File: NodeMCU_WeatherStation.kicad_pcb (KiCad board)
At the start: 2 copper layers, 75 x 93.5 mm, 24 parts, among them J1 AVR-ISP-6, J2 Conn_01x15, J3 Conn_01x15, J4 Conn_01x04, J5 Conn_01x04, U1 BME280, U2 ATmega328P-AU, U3 TLC555CD, Y1 16MHz

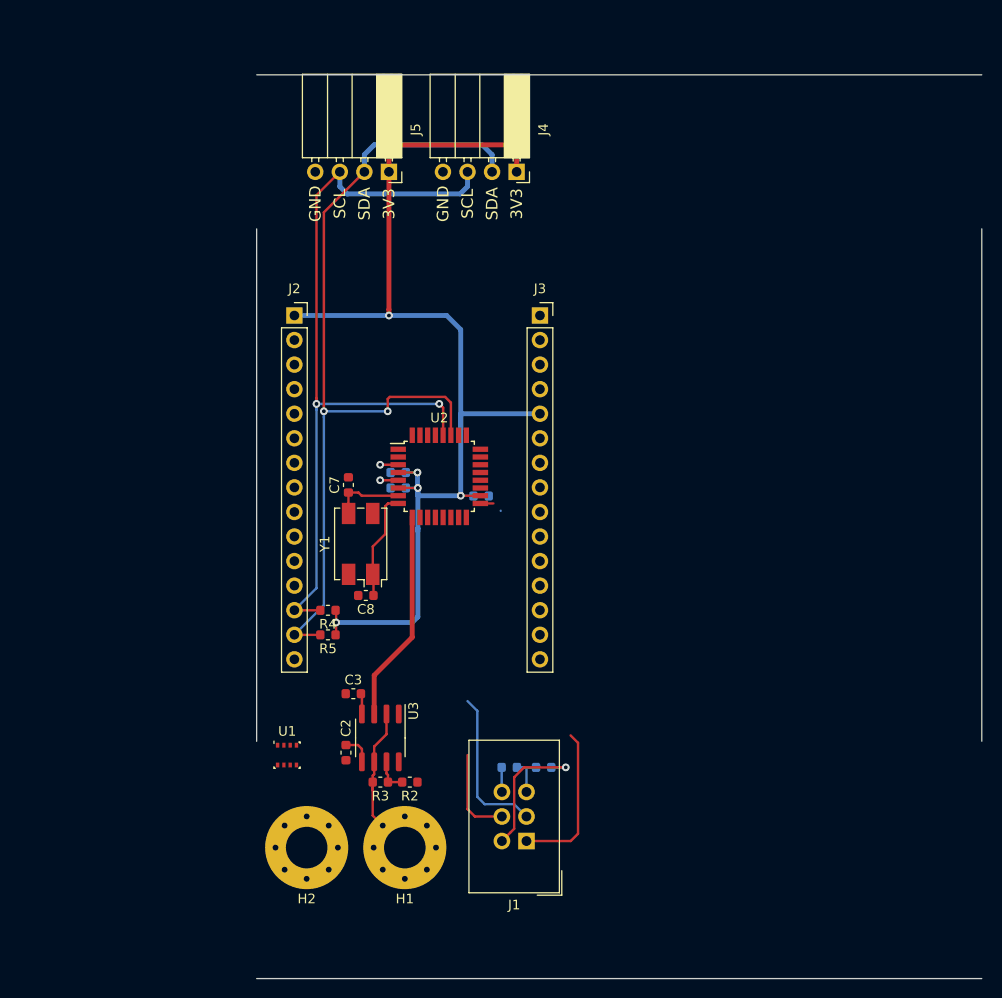
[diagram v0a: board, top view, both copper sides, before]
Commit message: added 4-20mA input and PT100 readout
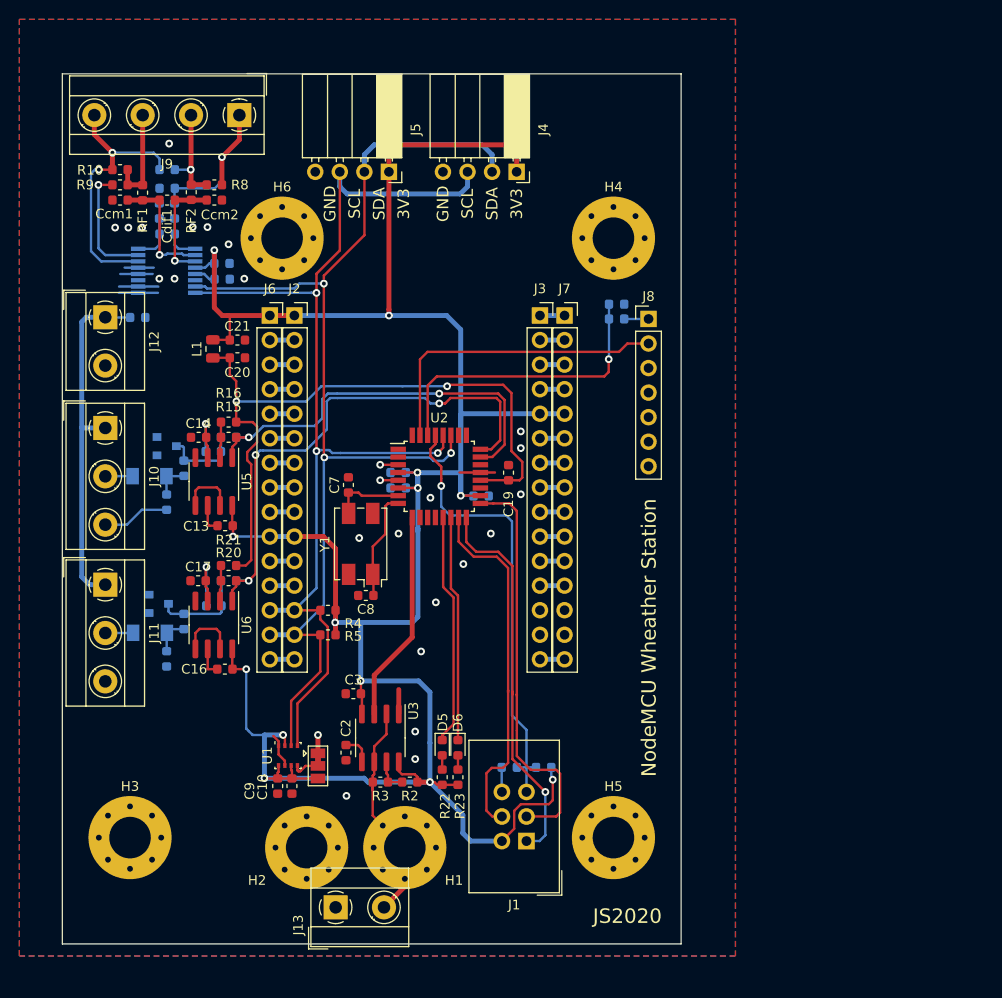
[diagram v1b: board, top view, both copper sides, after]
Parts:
- added C10: 100n, Capacitor_SMD:C_0603_1608Metric, F.Cu at (89.7, 128.7)
- added C11: 100n, Capacitor_SMD:C_0603_1608Metric, B.Cu at (82.5, 74.6)
- added C12: 100n, Capacitor_SMD:C_0603_1608Metric, B.Cu at (82.5, 76.2)
- added C13: 100n, Capacitor_SMD:C_0603_1608Metric, F.Cu at (82.8, 101.7)
- added C14: 100n, Capacitor_SMD:C_0603_1608Metric, F.Cu at (80.1, 92.6)
- added C15: 100n, Capacitor_SMD:C_0603_1608Metric, B.Cu at (83.2, 92.6)
- added C16: 100n, Capacitor_SMD:C_0603_1608Metric, F.Cu at (82.8, 116.6)
- added C17: 100n, Capacitor_SMD:C_0603_1608Metric, F.Cu at (80.0, 107.4)
- added C18: 100n, Capacitor_SMD:C_0603_1608Metric, B.Cu at (83.2, 107.4)
- added C19: 100n, Capacitor_SMD:C_0603_1608Metric, F.Cu at (112.1, 96.3)
- added C20: 100n, Capacitor_SMD:C_0603_1608Metric, F.Cu at (84.1, 84.4)
- added C21: 100n, Capacitor_SMD:C_0603_1608Metric, F.Cu at (84.1, 82.5)
- added C22: 100n, Capacitor_SMD:C_0603_1608Metric, B.Cu at (73.8, 80.2)
- added C9: 100n, Capacitor_SMD:C_0603_1608Metric, F.Cu at (88.3, 128.7)
- added Ccm1: 10n, Capacitor_SMD:C_0603_1608Metric, F.Cu at (72.0, 68.1)
- added Ccm2: 10n, Capacitor_SMD:C_0603_1608Metric, F.Cu at (81.7, 68.1)
- added Cdif1: 100n, Capacitor_SMD:C_0603_1608Metric, F.Cu at (76.8, 68.1)
- added Cdif2: 100n, Capacitor_SMD:C_0603_1608Metric, B.Cu at (76.8, 71.6)
- added D1: LL4148, Diode_SMD:D_MiniMELF, B.Cu at (75.0, 96.6)
- added D2: BZX84Cxx, Diode_SMD:D_SOT-23_ANK, B.Cu at (76.8, 93.5)
- added D3: LL4148, Diode_SMD:D_MiniMELF, B.Cu at (75.1, 112.8)
- added D4: BZX84Cxx, Diode_SMD:D_SOT-23_ANK, B.Cu at (76.0, 109.8)
- added D5: LED, LED_SMD:LED_0603_1608Metric, F.Cu at (105.3, 124.7)
- added D6: LED, LED_SMD:LED_0603_1608Metric, F.Cu at (106.9, 124.7)
- added H3: MountingHole_Pad, MountingHole:MountingHole_4.3mm_M4_Pad_Via, F.Cu at (73.0, 134.0)
- added H4: MountingHole_Pad, MountingHole:MountingHole_4.3mm_M4_Pad_Via, F.Cu at (123.0, 72.0)
- added H5: MountingHole_Pad, MountingHole:MountingHole_4.3mm_M4_Pad_Via, F.Cu at (123.0, 134.0)
- added H6: MountingHole_Pad, MountingHole:MountingHole_4.3mm_M4_Pad_Via, F.Cu at (88.7, 72.0)
- added J10: Screw_Terminal_01x03, TerminalBlock_MetzConnect:TerminalBlock_MetzConnect_Type055_RT01503HDWU_1x03_P5.00mm_Horizontal, F.Cu at (70.4, 91.6)
- added J11: Screw_Terminal_01x03, TerminalBlock_MetzConnect:TerminalBlock_MetzConnect_Type055_RT01503HDWU_1x03_P5.00mm_Horizontal, F.Cu at (70.4, 107.8)
- added J12: Screw_Terminal_01x02, TerminalBlock_MetzConnect:TerminalBlock_MetzConnect_Type055_RT01502HDWU_1x02_P5.00mm_Horizontal, F.Cu at (70.4, 80.2)
- added J13: Screw_Terminal_01x02, TerminalBlock_MetzConnect:TerminalBlock_MetzConnect_Type055_RT01502HDWU_1x02_P5.00mm_Horizontal, F.Cu at (94.3, 141.2)
- added J6: Conn_01x15, Connector_PinSocket_2.54mm:PinSocket_1x15_P2.54mm_Vertical, F.Cu at (87.5, 80.0)
- added J7: Conn_01x15, Connector_PinSocket_2.54mm:PinSocket_1x15_P2.54mm_Vertical, F.Cu at (117.9, 80.0)
- added J8: Conn_01x07, Connector_PinHeader_2.54mm:PinHeader_1x07_P2.54mm_Vertical, F.Cu at (126.6, 80.4)
- added J9: Screw_Terminal_01x04, TerminalBlock_MetzConnect:TerminalBlock_MetzConnect_Type055_RT01504HDWU_1x04_P5.00mm_Horizontal, F.Cu at (84.3, 59.3)
- added JP1: SolderJumper_3_Bridged12, Jumper:SolderJumper-3_P1.3mm_Bridged12_Pad1.0x1.5mm, F.Cu at (92.4, 126.6)
- added L1: L, Inductor_SMD:L_0805_2012Metric, F.Cu at (81.6, 83.5)
- added R10: n.b. (0R), Resistor_SMD:R_0603_1608Metric, F.Cu at (72.0, 64.9)
- added R11: n.b. (0R), Resistor_SMD:R_0603_1608Metric, B.Cu at (76.8, 64.9)
- added R12: 160, Resistor_SMD:R_0603_1608Metric, B.Cu at (76.8, 99.3)
- added R13: 100k, Resistor_SMD:R_0603_1608Metric, B.Cu at (78.6, 95.8)
- added R14: 100k, Resistor_SMD:R_0603_1608Metric, B.Cu at (81.6, 94.1)
- added R15: 15k, Resistor_SMD:R_0603_1608Metric, F.Cu at (83.2, 92.6)
- added R16: 75k, Resistor_SMD:R_0603_1608Metric, F.Cu at (83.2, 91.0)
- added R17: 160, Resistor_SMD:R_0603_1608Metric, B.Cu at (76.8, 115.5)
- added R18: 100k, Resistor_SMD:R_0603_1608Metric, B.Cu at (78.6, 111.6)
- added R19: 100k, Resistor_SMD:R_0603_1608Metric, B.Cu at (81.7, 110.0)
- added R20: 15k, Resistor_SMD:R_0603_1608Metric, F.Cu at (83.2, 107.4)
- added R21: 75k, Resistor_SMD:R_0603_1608Metric, F.Cu at (83.2, 105.9)
- added R22: R, Resistor_SMD:R_0603_1608Metric, F.Cu at (105.3, 127.8)
- added R23: R, Resistor_SMD:R_0603_1608Metric, F.Cu at (106.9, 127.8)
- added R6: 1k, Resistor_SMD:R_0603_1608Metric, B.Cu at (123.3, 80.4)
- added R7: 2k2, Resistor_SMD:R_0603_1608Metric, B.Cu at (123.3, 78.8)
- added R8: n.b. (0R), Resistor_SMD:R_0603_1608Metric, F.Cu at (81.7, 66.5)
- added R9: n.b. (0R), Resistor_SMD:R_0603_1608Metric, F.Cu at (72.0, 66.5)
- added RF1: 470, Resistor_SMD:R_0603_1608Metric, F.Cu at (74.3, 67.3)
- added RF2: 470, Resistor_SMD:R_0603_1608Metric, F.Cu at (79.3, 67.2)
- added RF3: 470, Resistor_SMD:R_0603_1608Metric, B.Cu at (77.6, 69.2)
- added RF4: 470, Resistor_SMD:R_0603_1608Metric, B.Cu at (76.0, 69.2)
- added Rref1: R, Resistor_SMD:R_0603_1608Metric, B.Cu at (76.8, 66.8)
- added U4: ADS122C04IPW, Package_SO:TSSOP-16_4.4x5mm_P0.65mm, B.Cu at (76.8, 75.4)
- added U5: LT1492, Package_SO:SOIC-8_3.9x4.9mm_P1.27mm, F.Cu at (81.7, 97.2)
- added U6: LT1492, Package_SO:SOIC-8_3.9x4.9mm_P1.27mm, F.Cu at (81.7, 112.0)
- moved U1 0.11 mm to (89.3, 125.5)
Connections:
- net Net-(U2-Pad25) renamed /I2C Water Sensor/ADC2
- net Net-(U2-Pad26) renamed /I2C Water Sensor/ADC3
- U1 pad 1: Net-(U1-Pad1) -> GND
- U1 pad 2: Net-(U1-Pad2) -> +3V3
- U1 pad 3: Net-(U1-Pad3) -> /SDA
- U1 pad 4: Net-(U1-Pad4) -> /SCL
- U1 pad 6: Net-(U1-Pad6) -> +3V3
- U1 pad 7: Net-(U1-Pad7) -> GND
- U1 pad 8: Net-(U1-Pad8) -> +3V3
- U2 pad 20: Net-(U2-Pad20) -> /4to20in 1/Vref
- U2 pad 23: Net-(U2-Pad23) -> /I2C Water Sensor/ADC0
- U2 pad 24: Net-(U2-Pad24) -> /I2C Water Sensor/ADC1
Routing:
- net +3V3: track 135.3 -> 276.3 mm, vias 6 -> 13
- net /4to20in 1/Vref: track 0.00 -> 70.4 mm, vias 0 -> 2
- net /I2C Water Sensor/ADC1: track 0.00 -> 54.6 mm, vias 0 -> 3
- net GND: track 6.50 -> 55.8 mm, vias 2 -> 26
- net /I2C Water Sensor/ADC0: track 0.00 -> 42.2 mm, vias 0 -> 2
- net /I2C Water Sensor/RESET: track 4.52 -> 46.6 mm, vias 0 -> 1
- net +24V: track 0.00 -> 36.8 mm
- net /I2C Water Sensor/TXD: track 0.00 -> 32.2 mm
- net /I2C Water Sensor/RXD: track 0.00 -> 31.5 mm, vias 0 -> 1
- net /SCL: track 83.0 -> 112.4 mm, vias 2 -> 3
- net /PT100 I2C readout/AIN3: track 0.00 -> 28.4 mm, vias 0 -> 2
- net /I2C Water Sensor/MOSI: track 9.46 -> 37.5 mm
- net /SDA: track 89.3 -> 115.5 mm, vias 2 -> 3
- net /I2C Water Sensor/SCK: track 17.6 -> 42.5 mm
- net Net-(D5-Pad1): track 0.00 -> 24.0 mm
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- added copper zone on B.Cu, net GND
- added copper zone on F.Cu, net GND
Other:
- board size 75 x 93.5 mm -> 64 x 90 mm
- board text added: "JS2020"
- board text added: "NodeMCU Wheather Station"

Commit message: added BPW34 for measurement of light intensity
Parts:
- added D7: BPW34, OptoDevice:Osram_DIL2_4.3x4.65mm_P5.08mm, F.Cu at (122.7, 96.3)
- added R24: 10k, Resistor_SMD:R_0603_1608Metric, F.Cu at (122.7, 88.5)
- R22, R23: value R -> 2k2
- moved J8 0.91 mm to (127.5, 80.4)
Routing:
- net /I2C Water Sensor/ADC2: track 0.00 -> 18.3 mm, vias 0 -> 1
- net /4to20in 1/Vref: track 70.4 -> 79.7 mm
- net /I2C Water Sensor/TXD: track 32.2 -> 33.7 mm
- net Net-(J8-Pad1): track 2.55 -> 3.46 mm
- net GND: vias 26 -> 38

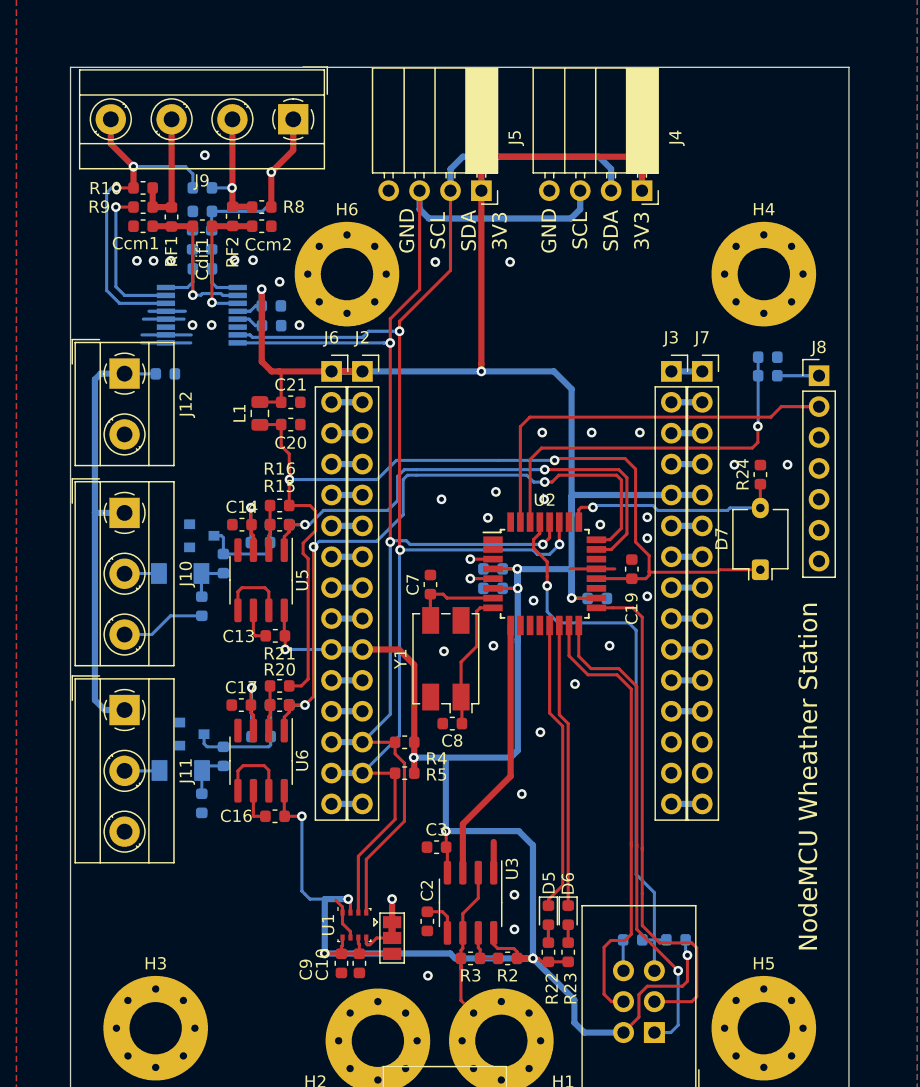
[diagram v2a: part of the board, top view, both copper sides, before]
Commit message: added digital output, 24V to 5V voltage regulator
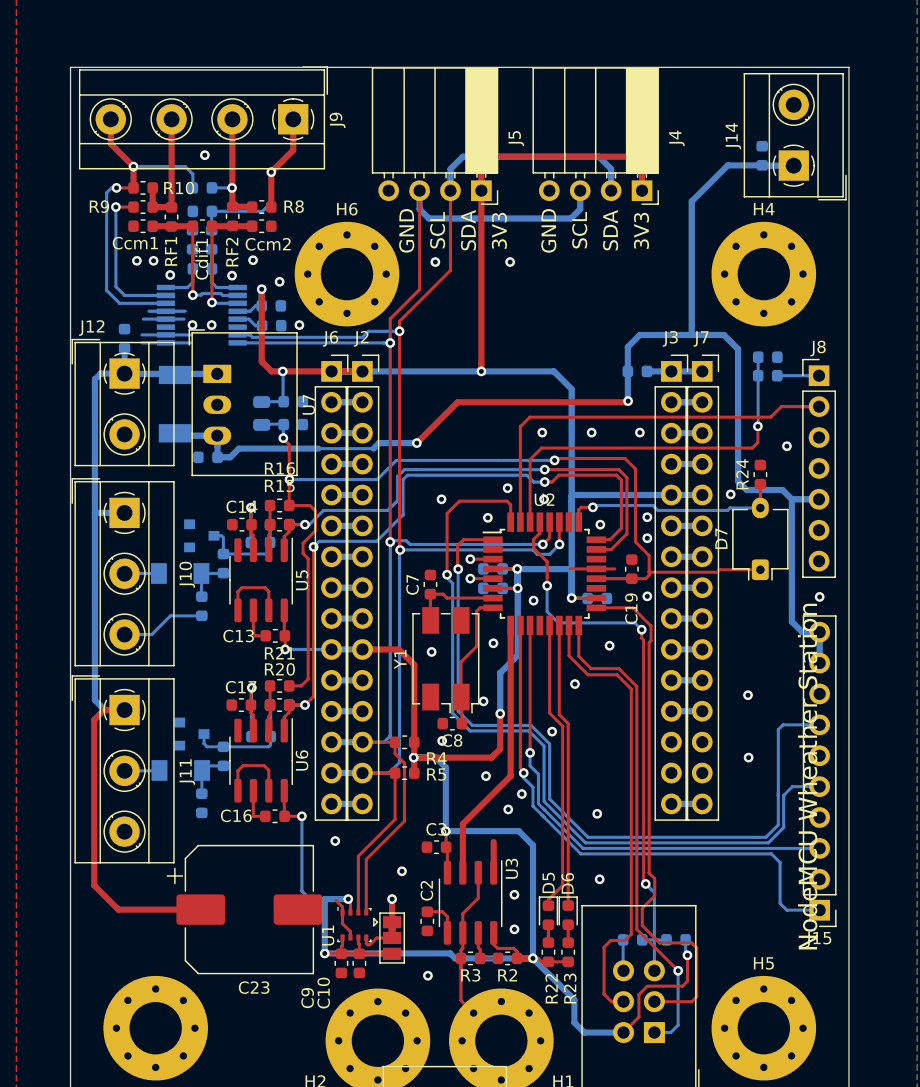
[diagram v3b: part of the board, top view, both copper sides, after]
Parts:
- added C23: 4u7, Capacitor_SMD:CP_Elec_10x10, F.Cu at (80.7, 124.2)
- added C24: 100n, Capacitor_SMD:C_0603_1608Metric, B.Cu at (77.3, 87.1)
- added C25: 100n, Capacitor_SMD:C_0603_1608Metric, B.Cu at (122.9, 62.3)
- added D8: SM4001, Diode_SMD:D_MELF, B.Cu at (74.6, 82.7)
- added J14: Screw_Terminal_01x02, TerminalBlock_MetzConnect:TerminalBlock_MetzConnect_Type055_RT01502HDWU_1x02_P5.00mm_Horizontal, F.Cu at (125.5, 63.1)
- added J15: Conn_01x10, Connector_PinHeader_2.54mm:PinHeader_1x10_P2.54mm_Vertical, F.Cu at (127.6, 124.3)
- added R25: 0R, Resistor_SMD:R_0603_1608Metric, B.Cu at (112.6, 80.0)
- added U7: R-785.0-0.5, Converter_DCDC:Converter_DCDC_RECOM_R-78E-0.5_THT, F.Cu at (78.1, 80.2)
- C20, C21, L1: moved to B.Cu
- Rref1: value R -> 1k65
- moved C22 4.43 mm to (70.4, 77.3), turned to 90 degrees
- moved C21 0.21 mm to (84.3, 82.5)
- moved C20 0.20 mm to (84.3, 84.4)
- moved L1 0.15 mm to (81.7, 83.5)
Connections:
- U2 pad 1: Net-(U2-Pad1) -> /I2C Water Sensor/DigIn2
- U2 pad 10: Net-(U2-Pad10) -> /I2C Water Sensor/DigOut1
- U2 pad 11: Net-(U2-Pad11) -> /I2C Water Sensor/DigOut2
- U2 pad 32: Net-(U2-Pad32) -> /I2C Water Sensor/DigIn1
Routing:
- net +5V: track 0.00 -> 110.3 mm, vias 0 -> 2
- net /I2C Water Sensor/DigIn1: track 0.00 -> 64.5 mm, vias 0 -> 1
- net /I2C Water Sensor/DigIn2: track 0.00 -> 62.1 mm, vias 0 -> 1
- net /I2C Water Sensor/DigOut1: track 0.00 -> 44.6 mm, vias 0 -> 1
- net /I2C Water Sensor/DigOut2: track 0.00 -> 39.8 mm, vias 0 -> 1
- net +24V: track 36.8 -> 72.5 mm
- net /NodeMCU/VIN: track 2.54 -> 4.55 mm
- net /SDA: track 115.5 -> 116.8 mm
- net +3V3: track 276.3 -> 277.3 mm, vias 13 -> 15
- net /SCL: track 112.4 -> 113.4 mm
- net /I2C Water Sensor/SCK: track 42.5 -> 43.3 mm
- net /I2C Water Sensor/RESET: track 46.6 -> 46.9 mm, vias 1 -> 3
- net /4to20in 1/Vref: track 79.7 -> 79.6 mm, vias 2 -> 3
- net GND: vias 38 -> 49
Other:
- board text added: "+24V"
- board text added: "+5V"
- board text added: "4-20mA"
- board text added: "PT100"
- board text added: "SDS011"
- board text added: "Water Electrodes"
